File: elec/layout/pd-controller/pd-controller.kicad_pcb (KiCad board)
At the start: 2 copper layers, 40 x 40 mm, 17 parts, among them Q1 MOSFET, U1 STUSB4500QTR

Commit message: ic layout complete
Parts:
- moved R1 15.6 mm to (142.0, 104.1), turned to 90 degrees
- moved R5 15.4 mm to (140.2, 97.0)
- moved R3 4.19 mm to (141.1, 104.1), turned to -90 degrees
- moved R6 3.36 mm to (144.9, 100.3)
- moved R2 3.30 mm to (140.0, 104.1), turned to -90 degrees
- moved C2 2.42 mm to (144.9, 97.5)
- moved R7 2.37 mm to (144.9, 98.9), turned to 90 degrees
- moved C3 0.13 mm to (142.3, 97.5)
- moved R4 0.12 mm to (144.0, 97.5)
- moved C4 0.10 mm to (141.2, 97.5)
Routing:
- net VBUS: track 0.00 -> 22.0 mm, vias 0 -> 11
- net GND: track 0.00 -> 12.7 mm, vias 0 -> 19
- net Q1-4-R5-1-R6-1-R7-1: track 5.93 -> 10.5 mm, vias 0 -> 2
- net VSINK_VCC: track 0.00 -> 2.35 mm
- net I2C_SCL: track 0.00 -> 1.36 mm
- net R1-2-U1-9: track 0.00 -> 1.26 mm
- net I2C_SDA: track 0.00 -> 1.09 mm
- net R6-2-U1-16: track 0.00 -> 1.07 mm
- net C2-1-R7-2: track 0.00 -> 0.95 mm
- added copper zone on B.Cu, net GND
- added copper zone on F.Cu, net GND
- added copper zone on B.Cu, net VBUS
- added copper zone on F.Cu, net VBUS
- added copper zone on F.Cu, net VSINK_VCC

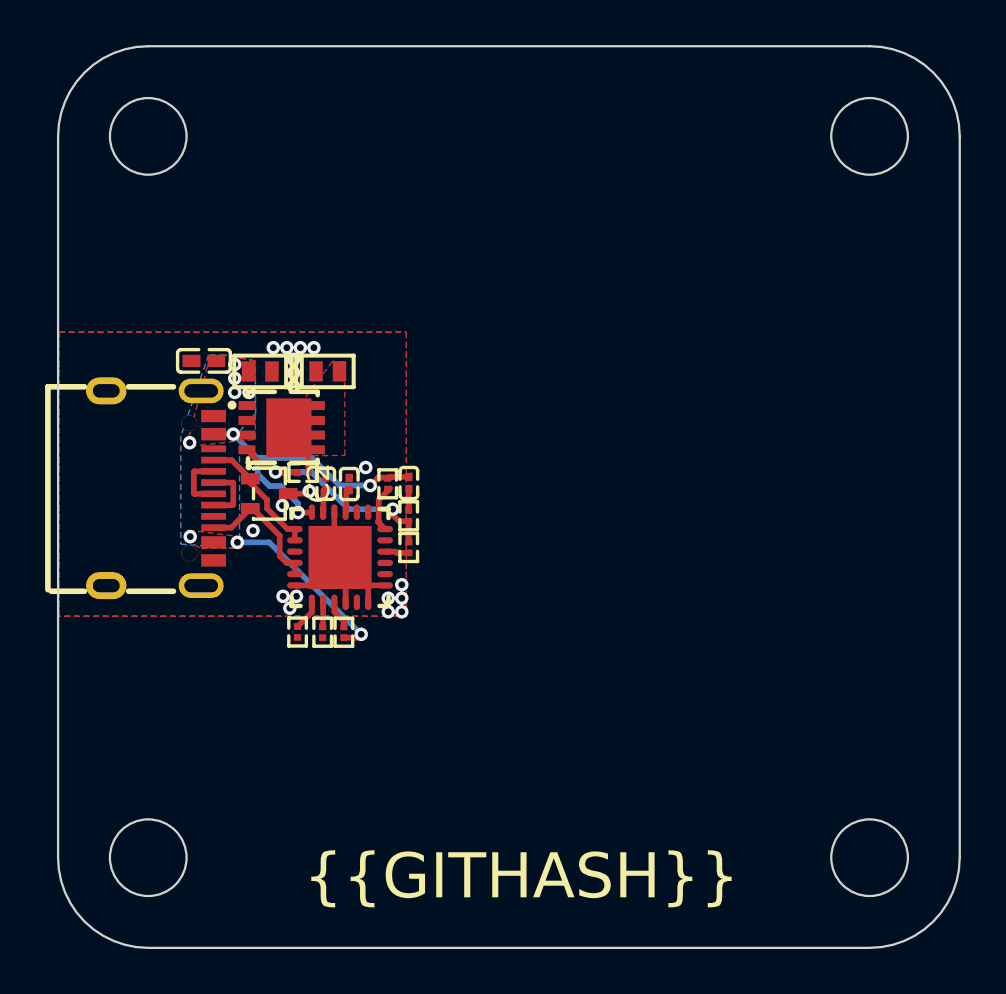
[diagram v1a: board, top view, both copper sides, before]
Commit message: add XT30 as output connector
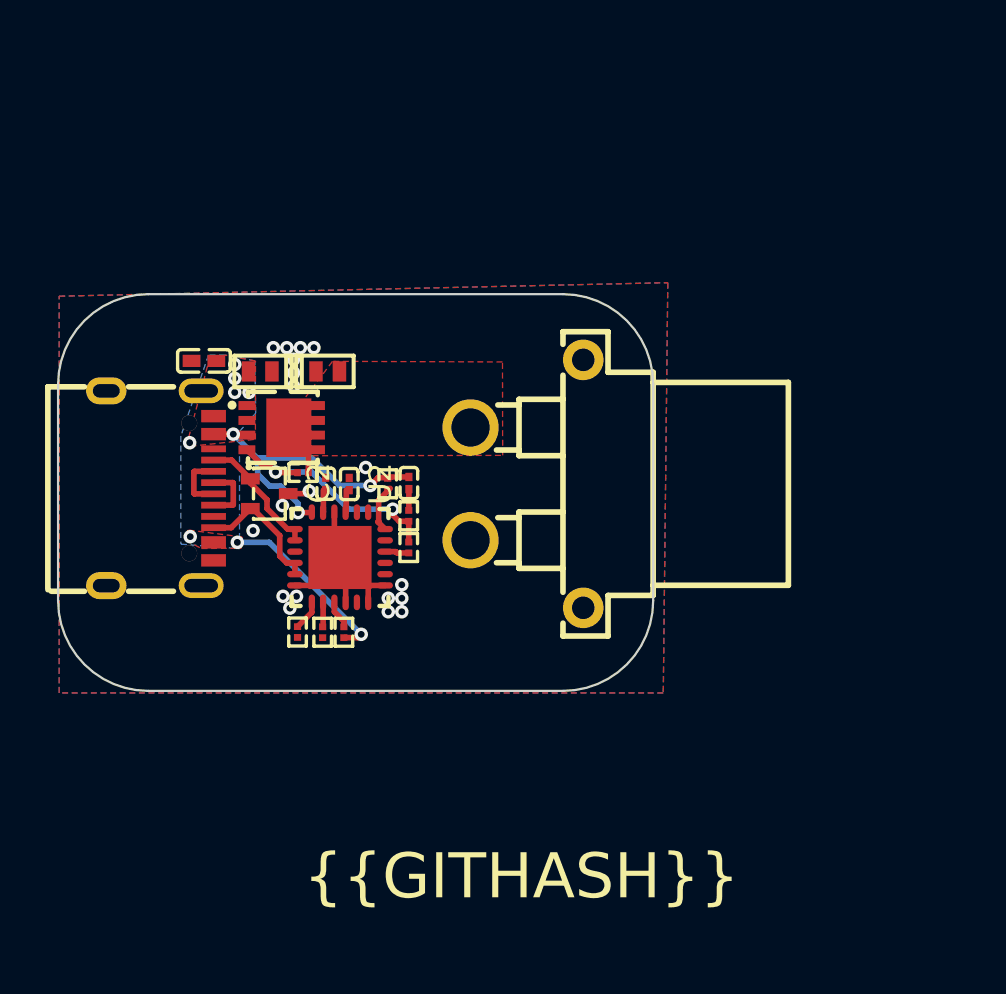
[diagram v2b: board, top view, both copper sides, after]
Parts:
- added U2: XT30PW, lcsc:CONN-TH_XT30PW-F-1, F.Cu at (150.2, 97.5)
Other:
- board size 40 x 40 mm -> 26.4 x 17.6 mm

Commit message: layout checkpoint
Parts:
- removed R4: 1kΩ ±1% 50mW, lcsc:R0201
- removed R5: 100kΩ ±1% 50mW, lcsc:R0201
- added CN1: STEMMA_RIGHT_ANGLE, lcsc:CONN-SMD_4P-P1.00_SM04B-SRSS-TB-LF-SN, F.Cu at (147.6, 104.1)
- added R8: 22.1kΩ ±1% 50mW, lcsc:R0201, F.Cu at (145.1, 100.3)
- added R9: 100Ω ±1% 50mW, lcsc:R0201, F.Cu at (145.1, 99.0)
- C1: value 4.7µF ±20% 10V X5R -> 4.7µF ±10% 35V X5R; footprint lcsc:C0402 -> lcsc:C0603
- R6: value 22.1kΩ ±1% 50mW -> 1kΩ ±1% 50mW
- R7: value 100Ω ±1% 50mW -> 100kΩ ±1% 50mW
- moved R7 5.09 mm to (140.2, 97.0), turned to 0 degrees
- moved R6 3.00 mm to (144.0, 97.5)
- moved C1 0.35 mm to (135.6, 91.8)
- moved U2 0.24 mm to (150.2, 97.3)
- moved C2 0.20 mm to (145.1, 97.5)
- moved R3 0.20 mm to (140.9, 104.1)
- turned D2 to 0 degrees
- turned D3 to 180 degrees
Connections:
- net R2-2-R3-2 renamed CN1-2-R2-2-R3-2
- C2 pad 1: C2-1-R7-2 -> C2-1-R9-2
- D2 pad 1: GND -> VBUS
- D2 pad 2: VBUS -> GND
- D3 pad 1: GND -> VSINK_VCC
- D3 pad 2: VSINK_VCC -> GND
- Q1 pad 4: Q1-4-R5-1-R6-1-R7-1 -> Q1-4-R7-1-R8-1-R9-1
- R6 pad 1: Q1-4-R5-1-R6-1-R7-1 -> VBUS
- R6 pad 2: R6-2-U1-16 -> R6-2-U1-18
- R7 pad 1: Q1-4-R5-1-R6-1-R7-1 -> Q1-4-R7-1-R8-1-R9-1
- R7 pad 2: C2-1-R7-2 -> VSINK_VCC
- U1 pad 16: R6-2-U1-16 -> R8-2-U1-16
- U1 pad 18: R4-2-U1-18 -> R6-2-U1-18
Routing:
- net I2C_SCL: track 1.36 -> 15.2 mm, vias 0 -> 2
- net Q1-4-R7-1-R8-1-R9-1: track 0.00 -> 11.7 mm, vias 0 -> 2
- net Q1-4-R5-1-R6-1-R7-1: track 10.5 -> 0.00 mm, vias 2 -> 0
- net I2C_SDA: track 1.09 -> 11.6 mm, vias 0 -> 2
- net CN1-2-R2-2-R3-2: track 0.00 -> 10.1 mm
- net R4-2-U1-18: track 2.16 -> 0.00 mm
- net R6-2-U1-18: track 0.00 -> 2.09 mm
- net R8-2-U1-16: track 0.00 -> 1.27 mm
- net R6-2-U1-16: track 1.07 -> 0.00 mm
- net C2-1-R9-2: track 0.00 -> 0.96 mm
- net C2-1-R7-2: track 0.95 -> 0.00 mm
- net GND: vias 19 -> 31

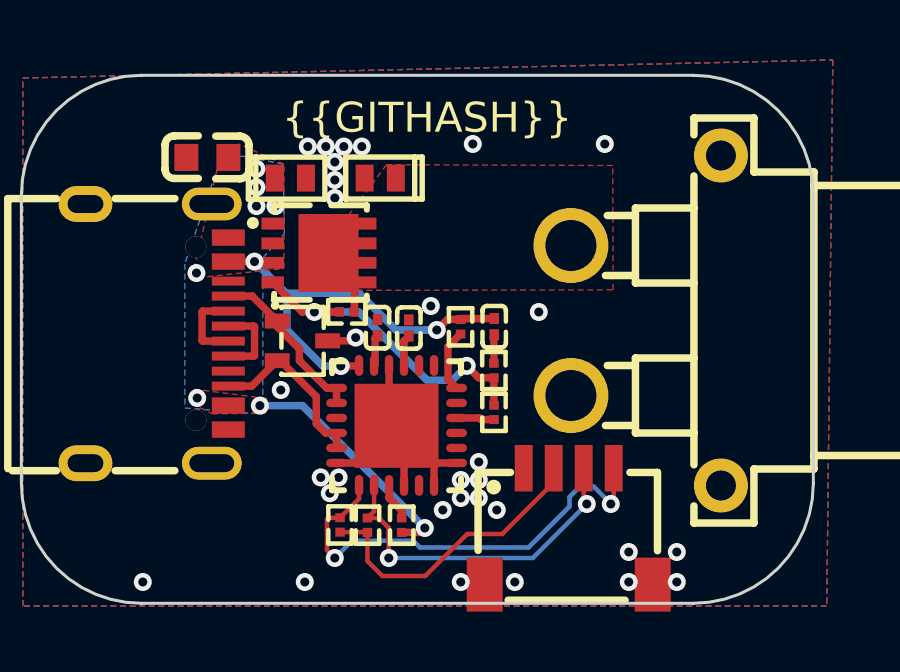
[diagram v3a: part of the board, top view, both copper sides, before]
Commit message: refactor to move components into their own files
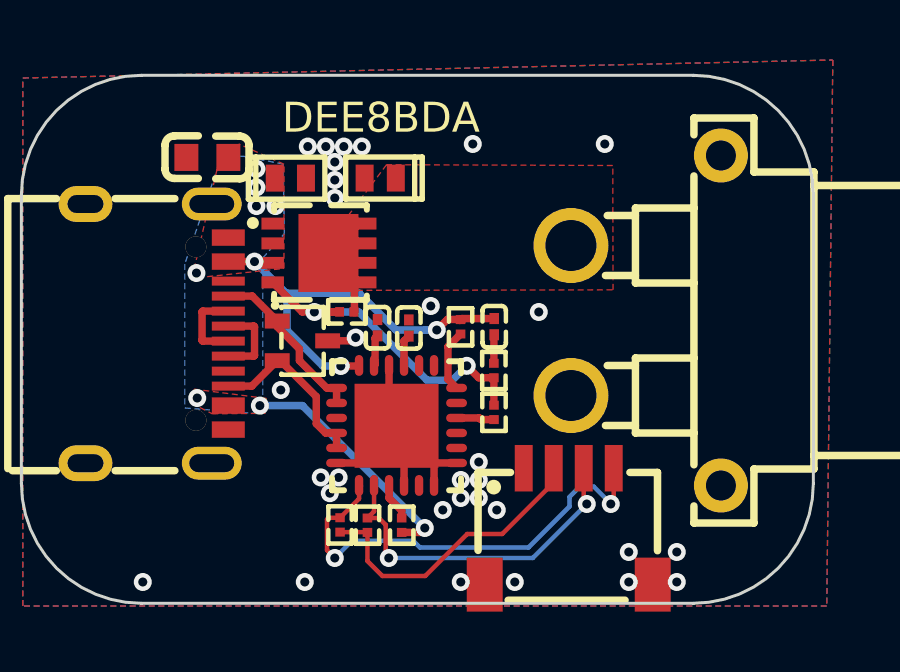
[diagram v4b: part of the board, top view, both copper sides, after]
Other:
- board text added: "DEE8BDA"
- board text added: "USBPD DEV BOARD"
- board text removed: "{{GITHASH}}"

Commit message: update layout
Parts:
- removed R8: 22.1kΩ ±1% 50mW, lcsc:R0201
- removed R9: 100Ω ±1% 50mW, lcsc:R0201
- added R4: 1kΩ ±1% 50mW, lcsc:R0201, F.Cu at (143.8, 97.8)
- added R5: 100kΩ ±1% 50mW, lcsc:R0201, F.Cu at (145.7, 99.0)
- R6: value 1kΩ ±1% 50mW -> 22.1kΩ ±1% 50mW
- R7: value 100kΩ ±1% 50mW -> 100Ω ±1% 50mW
- moved R7 5.20 mm to (145.0, 99.0), turned to 90 degrees
- moved R6 2.79 mm to (145.0, 100.1)
- moved C2 0.36 mm to (145.0, 97.8)
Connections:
- C2 pad 1: C2-1-R9-2 -> C2-1-R7-2
- Q1 pad 4: Q1-4-R7-1-R8-1-R9-1 -> Q1-4-R5-1-R6-1-R7-1
- R6 pad 1: VBUS -> Q1-4-R5-1-R6-1-R7-1
- R6 pad 2: R6-2-U1-18 -> R6-2-U1-16
- R7 pad 1: Q1-4-R7-1-R8-1-R9-1 -> Q1-4-R5-1-R6-1-R7-1
- R7 pad 2: VSINK_VCC -> C2-1-R7-2
- U1 pad 16: R8-2-U1-16 -> R6-2-U1-16
- U1 pad 18: R6-2-U1-18 -> R4-2-U1-18
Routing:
- net Q1-4-R5-1-R6-1-R7-1: track 0.00 -> 12.1 mm, vias 0 -> 2
- net Q1-4-R7-1-R8-1-R9-1: track 11.7 -> 0.00 mm, vias 2 -> 0
- net VSINK_VCC: track 2.35 -> 7.14 mm
- net R6-2-U1-18: track 2.09 -> 0.00 mm
- net R4-2-U1-18: track 0.00 -> 1.52 mm
- net R8-2-U1-16: track 1.27 -> 0.00 mm
- net R6-2-U1-16: track 0.00 -> 1.22 mm
- net C2-1-R9-2: track 0.96 -> 0.00 mm
- net C2-1-R7-2: track 0.00 -> 0.66 mm
- net GND: vias 31 -> 30
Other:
- board text added: "{{GITHASH}}"
- board text removed: "DEE8BDA"

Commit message: layout sync working
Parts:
- removed CN1: STEMMA_RIGHT_ANGLE, lcsc:CONN-SMD_4P-P1.00_SM04B-SRSS-TB-LF-SN
- removed U2: XT30PW, lcsc:CONN-TH_XT30PW-F-1
- C3: value 1µF ±20% 6.3V X5R -> (none)
- Q1: footprint lcsc:PDFN3333-8_L3.1-W3.2-P0.65-LS3.4-BL -> lcsc:SOT-23-3_L2.9-W1.3-P1.90-LS2.4-BR
- R3: value 4.64kΩ ±1% 50mW -> (none)
- R4: value 1kΩ ±1% 50mW -> (none)
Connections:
- net C2-1-R7-2 renamed net
- net CN1-2-R2-2-R3-2 renamed hv
- net GND renamed lv
- net R1-2-U1-9 renamed net-3
- net R4-2-U1-18 renamed net-2
- net R6-2-U1-16 renamed net-4
- net U1-11 renamed attach
- net U1-14 renamed power_ok3
- net U1-15 renamed gpio
- net U1-17 renamed a_b_side
- net U1-19 renamed alert
- net U1-20 renamed power_ok2
- net U1-3 renamed PD_CONTROLLER.footprint.pins[18].net-net
- net USB1-3 renamed USB_CONNECTOR-signal-1
- net USB1-5-USB1-7 renamed USB_CONNECTOR-net-1
- net USB1-6-USB1-8 renamed USB_CONNECTOR-net
- net USB1-9 renamed USB_CONNECTOR-signal
- Q1 pad 1: VBUS -> net-1
- Q1 pad 3: VBUS -> VSINK_VCC
- R5 pad 1: Q1-4-R5-1-R6-1-R7-1 -> net-1
- R6 pad 1: Q1-4-R5-1-R6-1-R7-1 -> net-1
- R7 pad 1: Q1-4-R5-1-R6-1-R7-1 -> net-1
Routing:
- net (no net): track 0.00 -> 22.2 mm, vias 0 -> 2
- net Q1-4-R5-1-R6-1-R7-1: track 12.1 -> 0.00 mm, vias 2 -> 0
- net hv: track 10.1 -> 0.00 mm
- net net-1: track 0.00 -> 1.22 mm
- net net: track 0.66 -> 0.00 mm
- net net-3: track 1.26 -> 0.66 mm

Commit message: delete unused modules and add library parts
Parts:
- C3: value (none) -> 1µF ±20% 6.3V X5R
- C4: value 1µF ±20% 6.3V X5R -> (none)
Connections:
- C2 pad 1: net -> net-4
- Q1 pad 1: net-1 -> net-3
- R1 pad 2: net-3 -> net-1
- R5 pad 1: net-1 -> net-3
- R6 pad 1: net-1 -> net-3
- R6 pad 2: net-4 -> net
- R7 pad 1: net-1 -> net-3
- R7 pad 2: net -> net-4
- U1 pad 16: net-4 -> net
- U1 pad 9: net-3 -> net-1
- USB1 pad 3: USB_CONNECTOR-signal-1 -> USB_CONNECTOR-signal
- USB1 pad 5: USB_CONNECTOR-net-1 -> USB_CONNECTOR-net
- USB1 pad 6: USB_CONNECTOR-net -> USB_CONNECTOR-net-1
- USB1 pad 7: USB_CONNECTOR-net-1 -> USB_CONNECTOR-net
- USB1 pad 8: USB_CONNECTOR-net -> USB_CONNECTOR-net-1
- USB1 pad 9: USB_CONNECTOR-signal -> USB_CONNECTOR-signal-1
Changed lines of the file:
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@@
             (layers "F.Cu" "F.Paste" "F.Mask")
             (remove_unused_layers no)
-            (net 26 "net-1")
+            (net 23 "net-3")
 )
         (pad "2" smd rect
@@
             (layers "F.Cu" "F.Paste" "F.Mask")
             (remove_unused_layers no)
-            (net 24 "net-4")
+            (net 20 "net")
 )
         (model "/Users/napowderly/Projects/nonos/build/kicad/libs/3dmodels/lcsc.3dshapes/R0201_L0.6-W0.3-H0.3.wrl"
@@
             (layers "F.Cu" "F.Paste" "F.Mask")
             (remove_unused_layers no)
-            (net 1 "USB_CONNECTOR-signal-1")
+            (net 2 "USB_CONNECTOR-signal")
 )
         (pad "4" smd rect
@@
             (layers "F.Cu" "F.Paste" "F.Mask")
             (remove_unused_layers no)
-            (net 3 "USB_CONNECTOR-net-1")
+            (net 4 "USB_CONNECTOR-net")
 )
         (pad "6" smd rect
@@
             (layers "F.Cu" "F.Paste" "F.Mask")
             (remove_unused_layers no)
-            (net 4 "USB_CONNECTOR-net")
+            (net 3 "USB_CONNECTOR-net-1")
 )
         (pad "7" smd rect
@@
             (layers "F.Cu" "F.Paste" "F.Mask")
             (remove_unused_layers no)
-            (net 3 "USB_CONNECTOR-net-1")
+            (net 4 "USB_CONNECTOR-net")
 )
         (pad "8" smd rect
@@
             (layers "F.Cu" "F.Paste" "F.Mask")
             (remove_unused_layers no)
-            (net 4 "USB_CONNECTOR-net")
+            (net 3 "USB_CONNECTOR-net-1")
 )
         (pad "9" smd rect
@@
             (layers "F.Cu" "F.Paste" "F.Mask")
             (remove_unused_layers no)
-            (net 2 "USB_CONNECTOR-signal")
+            (net 1 "USB_CONNECTOR-signal-1")
 )
         (pad "10" smd rect
@@
             (layers "F.Cu" "F.Paste" "F.Mask")
             (remove_unused_layers no)
-            (net 23 "net-3")
+            (net 26 "net-1")
 )
         (pad "10" smd oval
@@
             (layers "F.Cu" "F.Paste" "F.Mask")
             (remove_unused_layers no)
-            (net 24 "net-4")
+            (net 20 "net")
 )
         (pad "17" smd oval
@@
             (layers "F.Cu" "F.Paste" "F.Mask")
             (remove_unused_layers no)
-            (net 20 "net")
+            (net 24 "net-4")
 )
         (pad "2" smd rect
@@
             (layers "F.Cu" "F.Paste" "F.Mask")
             (remove_unused_layers no)
-            (net 26 "net-1")
+            (net 23 "net-3")
 )
         (pad "2" smd rect
@@
             (layers "F.Cu" "F.Paste" "F.Mask")
             (remove_unused_layers no)
-            (net 20 "net")
+            (net 24 "net-4")
 )
         (model "/Users/napowderly/Projects/nonos/build/kicad/libs/3dmodels/lcsc.3dshapes/R0201_L0.6-W0.3-H0.3.wrl"
@@
             (layers "F.Cu" "F.Paste" "F.Mask")
             (remove_unused_layers no)
-            (net 26 "net-1")
+            (net 23 "net-3")
 )
         (pad "2" smd rect
@@
                     (thickness 0.15))
                 (hide no)))
-        (property "Value" "1µF ±20% 6.3V X5R"
+        (property "Value" ""
             (at 0 4 90)
             (layer "F.Fab")
@@
                     (thickness 0.15))
                 (hide no)))
-        (property "Value" ""
+        (property "Value" "1µF ±20% 6.3V X5R"
             (at 0 4 90)
             (layer "F.Fab")
@@
             (layers "F.Cu" "F.Paste" "F.Mask")
             (remove_unused_layers no)
-            (net 23 "net-3")
+            (net 26 "net-1")
 )
         (model "/Users/napowderly/Projects/nonos/build/kicad/libs/3dmodels/lcsc.3dshapes/R0201_L0.6-W0.3-H0.3.wrl"
@@
             (layers "F.Cu" "F.Paste" "F.Mask")
             (remove_unused_layers no)
-            (net 26 "net-1")
+            (net 23 "net-3")
 )
         (pad "2" smd rect
